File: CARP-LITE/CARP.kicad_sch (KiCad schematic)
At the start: 103 parts, among them J1 USB-C, J10 PYRO_2, J3 I2C1+3V3, J4 2S XT30, J5 UART+5V+I2C1, J6 PYRO_1, J8 PWM1+6V, J9 PWM2+6V, Q5 SQ2318CES, Q6 SQ2318CES, Q7 SQ2318CES, SW1 SW_Push, SW2 SW_Push, U1 W25Q128JVSIMTR (16MB), U2 W25Q32RVXHJQ (2MB), U3 3V3 LDO, U4 RP2350_60QFN, U5 LSM6DSO, U6 BMP390, U7 5V LDO, U8 6V LDO, Y1 ABM8-272-T3

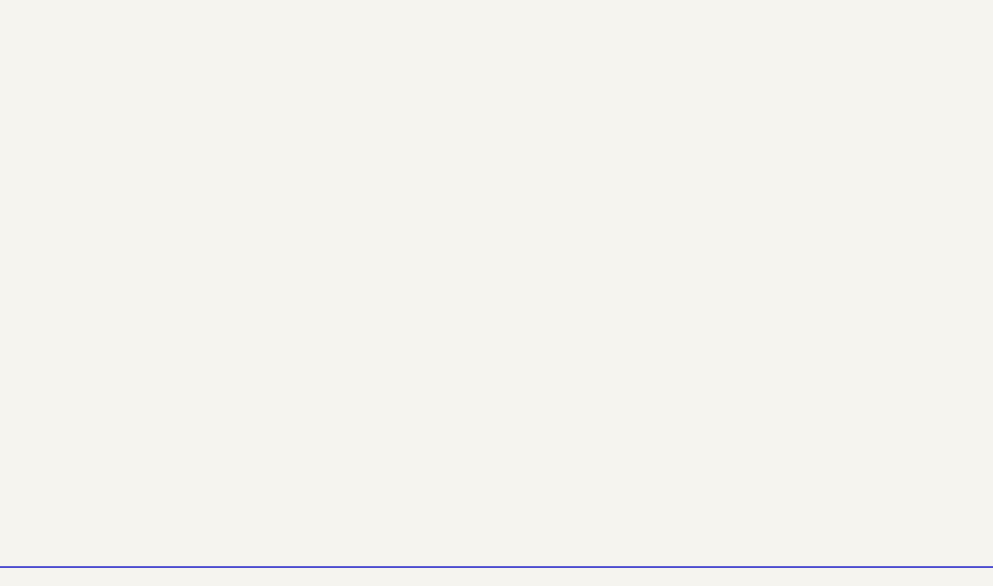
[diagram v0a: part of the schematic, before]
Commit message: Add preliminary buck design
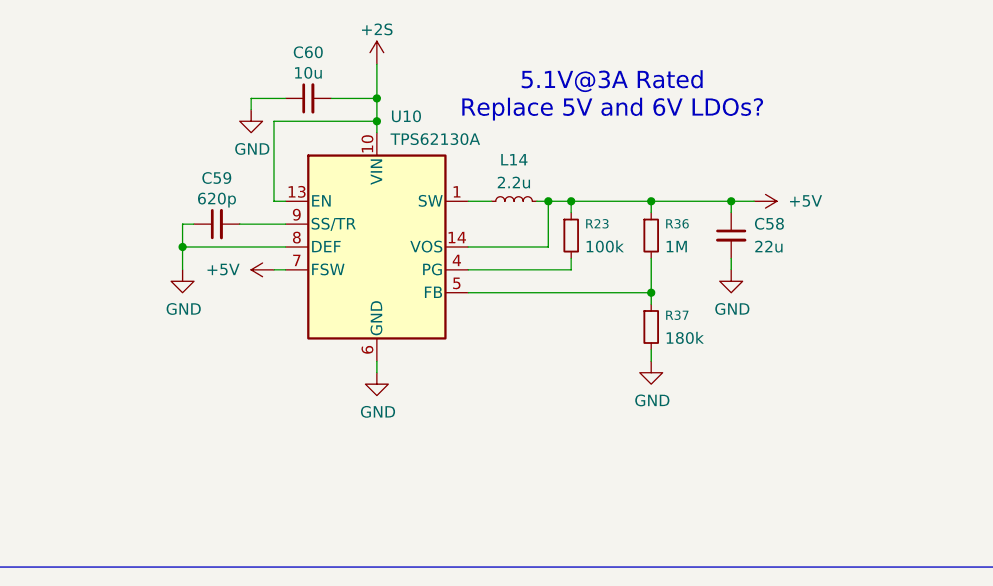
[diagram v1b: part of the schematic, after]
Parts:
- added C58: 22u, Capacitor_SMD:C_0805_2012Metric, symbol Device:C_Small
- added C59: 620p, Capacitor_SMD:C_0402_1005Metric, symbol Device:C_Small
- added C60: 10u, Capacitor_SMD:C_0805_2012Metric, symbol Device:C_Small
- added L14: 2.2u, Inductor_SMD:L_Coilcraft_XxL4020, symbol Device:L_Small
- added R23: 100k, symbol Device:R_Small
- added R36: 1M, symbol Device:R_Small
- added R37: 180k, symbol Device:R_Small
- added U10: TPS62130A, Package_DFN_QFN:VQFN-16-1EP_3x3mm_P0.5mm_EP1.68x1.68mm_ThermalVias, symbol Regulator_Switching:TPS62130A
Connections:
- net +2S: now also C60.2, U10.10 (VIN), U10.11 (VIN), U10.12 (VIN), U10.13 (EN)
- net +5V: now also C58.1, L14.2, R23.1, R36.1, U10.14 (VOS), U10.7 (FSW)
- net GND: now also C58.2, C59.1, C60.1, R37.2, U10.15 (GND), U10.16 (GND), U10.17 (GND), U10.6 (GND), U10.8 (DEF)
- new net: R36.2, R37.1, U10.5 (FB)
- new net: R23.2, U10.4 (PG)
- new net: C59.2, U10.9 (SS/TR)
- new net: L14.1, U10.1 (SW), U10.2 (SW), U10.3 (SW)
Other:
- note added: "5.1V@3A Rated Replace 5V and 6V LDOs?"

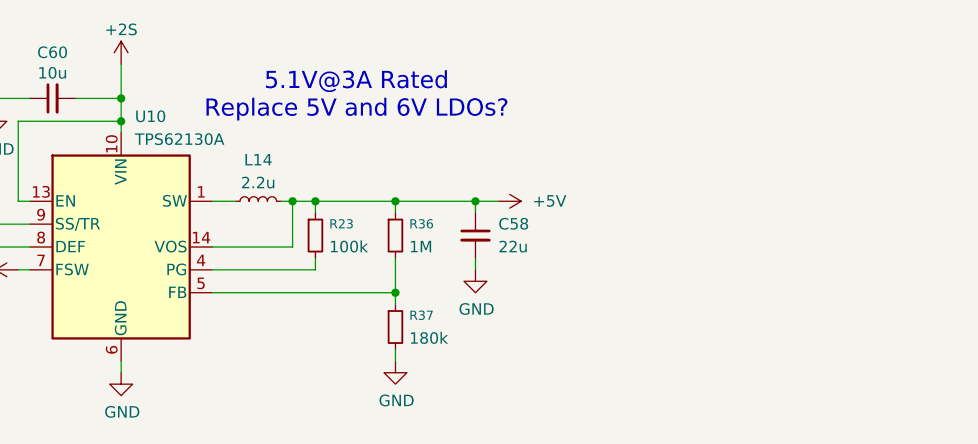
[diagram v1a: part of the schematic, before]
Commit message: add link to sim
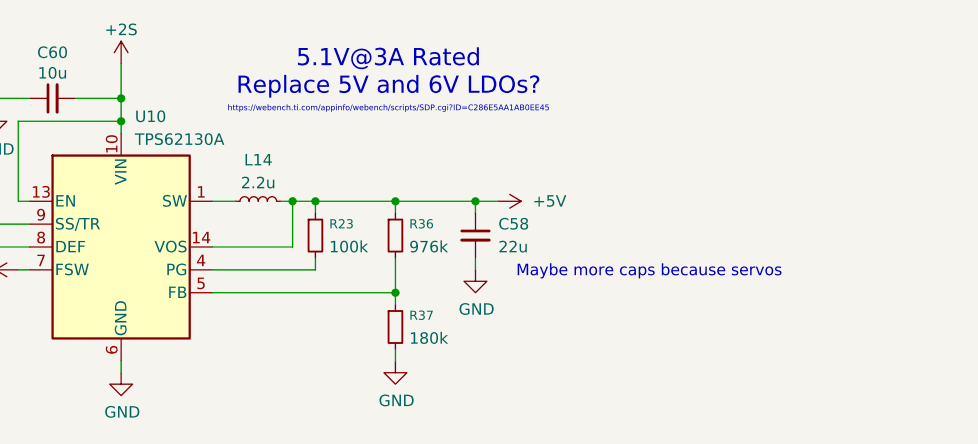
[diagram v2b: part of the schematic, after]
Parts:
- L14: MFR XEL4020-222MEB -> XGL4020-222MEC
- R36: value 1M -> 976k
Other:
- note added: "Maybe more caps because servos"
- note added: "https://webench.ti.com/appinfo/webench/scripts/SDP.cgi?ID=C286E5AA1AB0EE45"
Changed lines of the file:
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@@
 	(text "5.1V@3A Rated\nReplace 5V and 6V LDOs?"
 		(exclude_from_sim no)
-		(at 96.012 -38.354 0)
+		(at 99.568 -40.894 0)
 		(effects
 			(font
@@
 		)
 	)
+	(text "https://webench.ti.com/appinfo/webench/scripts/SDP.cgi?ID=C286E5AA1AB0EE45"
+		(exclude_from_sim no)
+		(at 99.568 -36.83 0)
+		(effects
+			(font
+				(size 0.635 0.635)
+			)
+		)
+	)
 	(text "info for choosing an NMOS:\n1.5v max gate threshold voltage\non-resistance: V_gs 2.5V or 1.8V (NO FET)\nV_ds 20V minimum"
 		(exclude_from_sim no)
@@
 		)
 	)
+	(text "Maybe more caps because servos\n"
+		(exclude_from_sim no)
+		(at 128.524 -18.796 0)
+		(effects
+			(font
+				(size 1.27 1.27)
+			)
+		)
+	)
 	(text "Power Delivery"
 		(exclude_from_sim no)
@@
 	)
 	(junction
-		(at 88.9 -26.67)
-		(diameter 0)
-		(color 0 0 0 0)
-	)
-	(junction
 		(at 303.53 26.67)
 		(diameter 0)
@@
 	)
 	(junction
+		(at 88.9 -26.67)
+		(diameter 0)
+		(color 0 0 0 0)
+	)
+	(junction
 		(at 334.01 237.49)
 		(diameter 0)
@@
 			)
 		)
-		(property "Value" "1M"
+		(property "Value" "976k"
 			(at 101.854 -21.59 0)
 			(show_name no)
@@
 			)
 		)
-		(property "MFR" "XEL4020-222MEB"
+		(property "MFR" "XGL4020-222MEC"
 			(at 85.09 -26.67 90)
 			(hide yes)

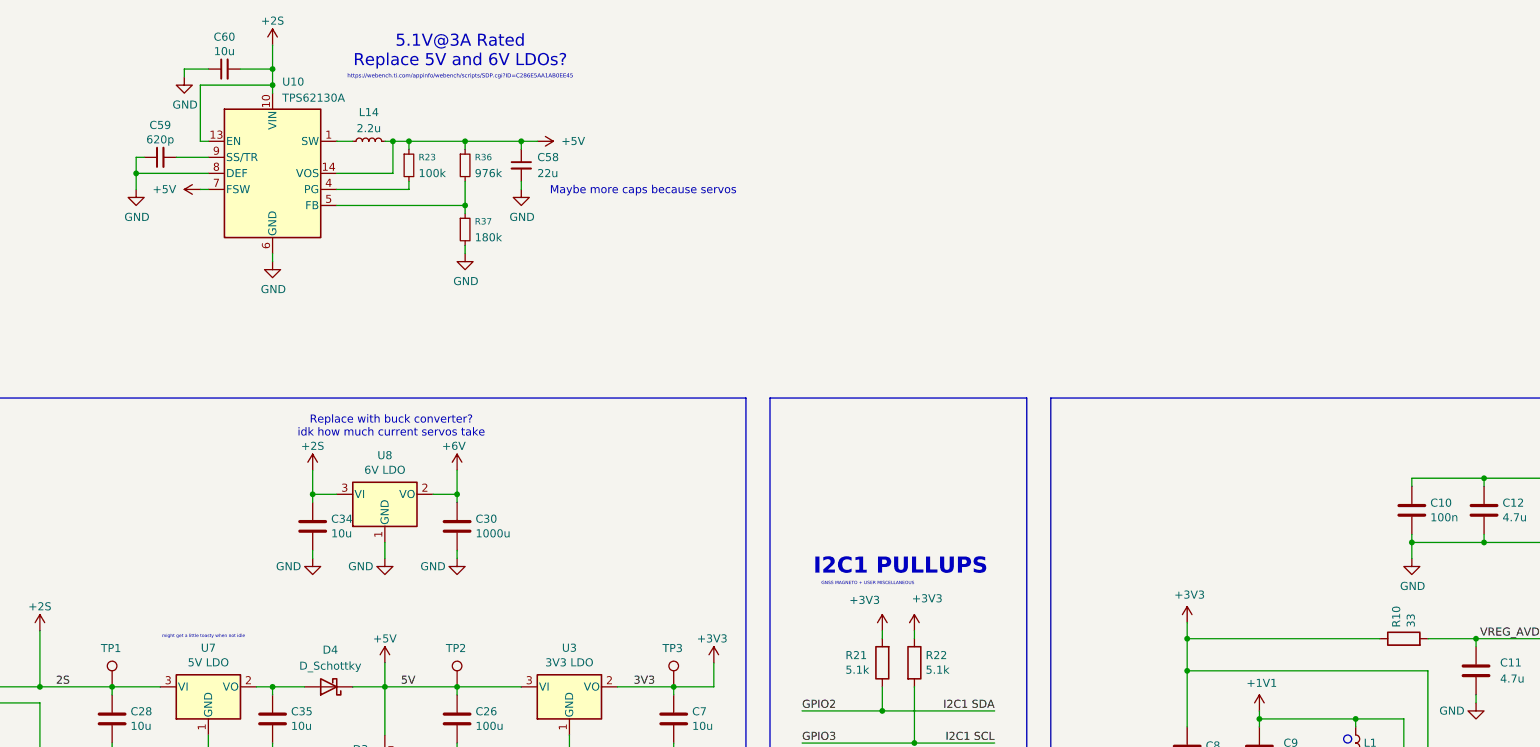
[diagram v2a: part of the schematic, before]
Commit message: move stuff around
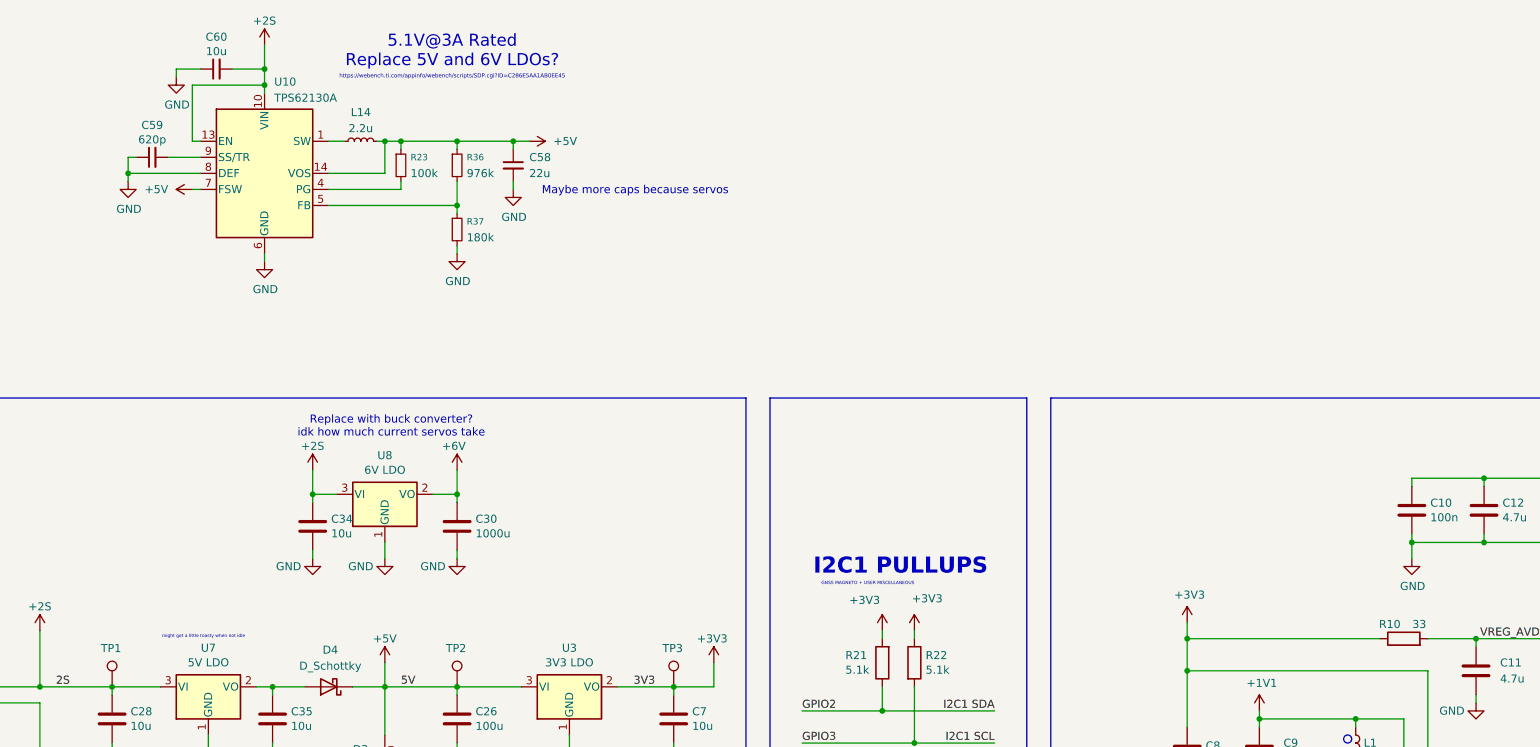
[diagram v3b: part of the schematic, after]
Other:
- moved on the sheet: C58, C59, C60, L14, R23, R36, R37, U10

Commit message: power delivery revamp
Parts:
- removed C28, C35: 10u, Capacitor_SMD:C_0603_1608Metric, symbol Device:C
- removed U7: 5V LDO, Package_TO_SOT_SMD:SOT-223-3_TabPin2, symbol Regulator_Linear:NCP1117-3.3_SOT223
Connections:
- net +2S: no longer TP1.1
- net +5V: now also R16.1; no longer C58.1, L14.2, R23.1, R36.1, U10.14 (VOS), U10.7 (FSW)
- net VBUS: no longer R16.1
- net +5V1: now reaches D4.2 (A)
- net +5V1: now also C58.1, L14.2, R23.1, R36.1, TP1.1, U10.14 (VOS), U10.7 (FSW)
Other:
- note added: "5.1V@3A Rated"
- note added: "more caps"
- note removed: "5.1V@3A Rated Replace 5V and 6V LDOs?"
- note removed: "Maybe more caps because servos"
- note removed: "might get a little toasty when not idle"
- moved on the sheet: C26, C29, C30, C34, C58, C59, C60, C7, J4, L14, R17, R18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

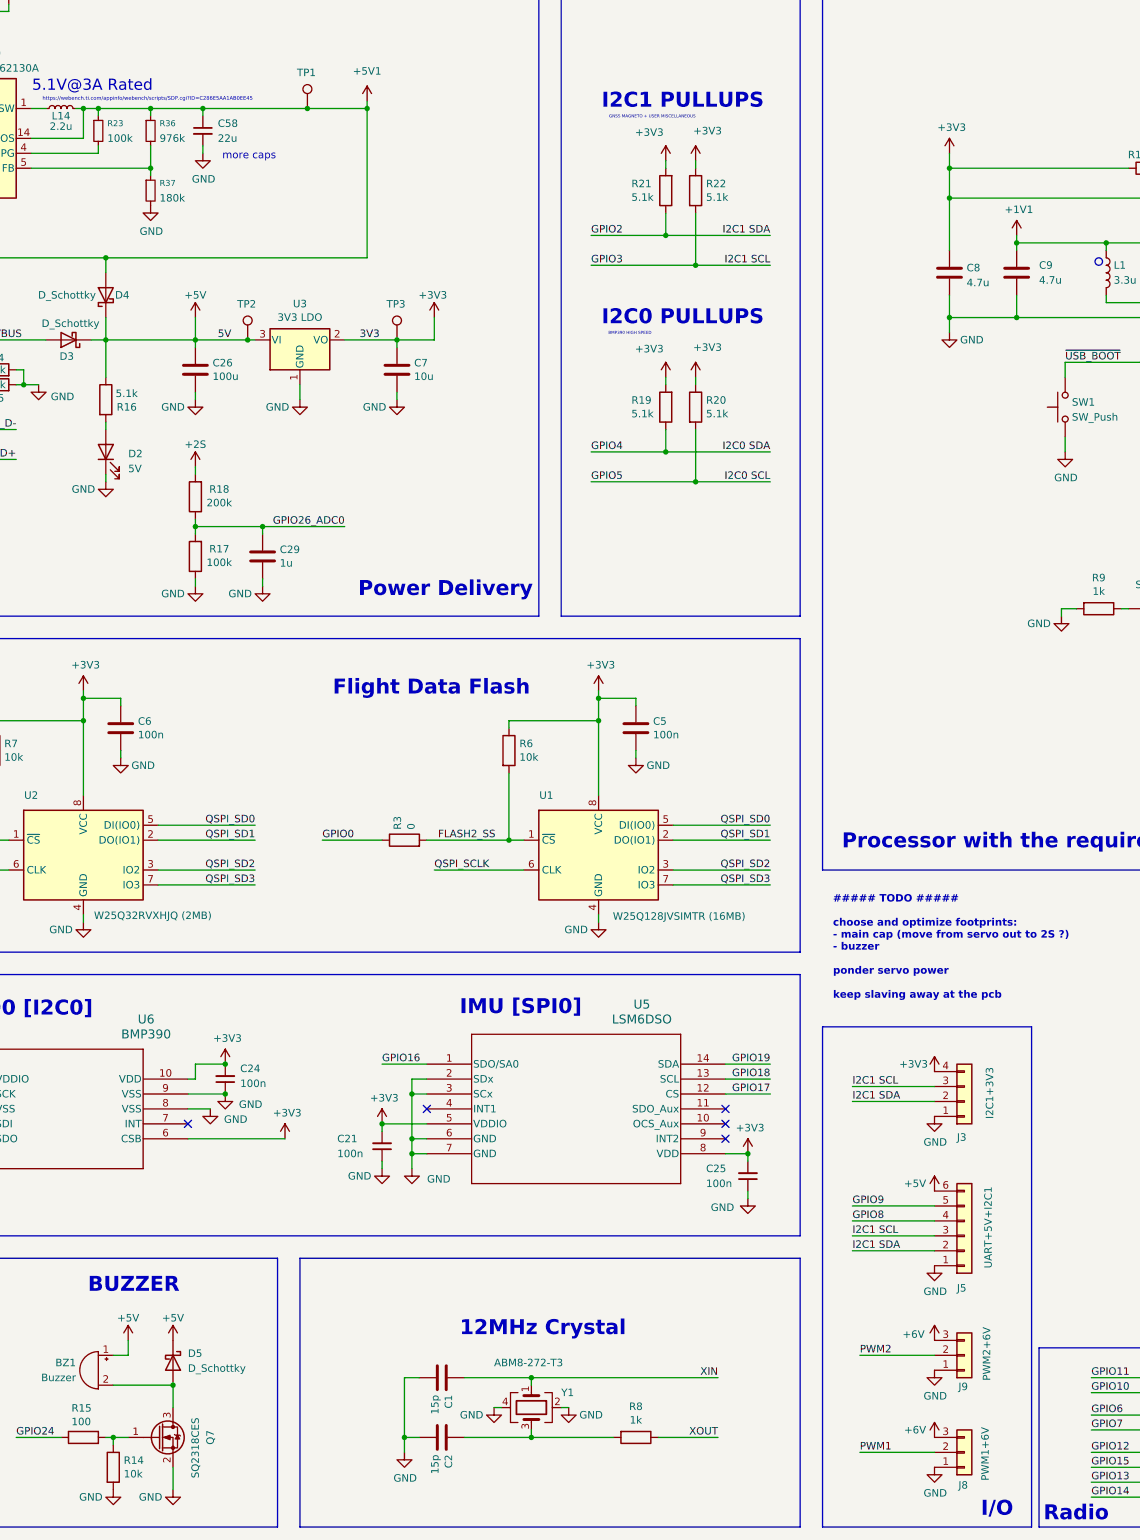
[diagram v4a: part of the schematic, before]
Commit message: add tantals
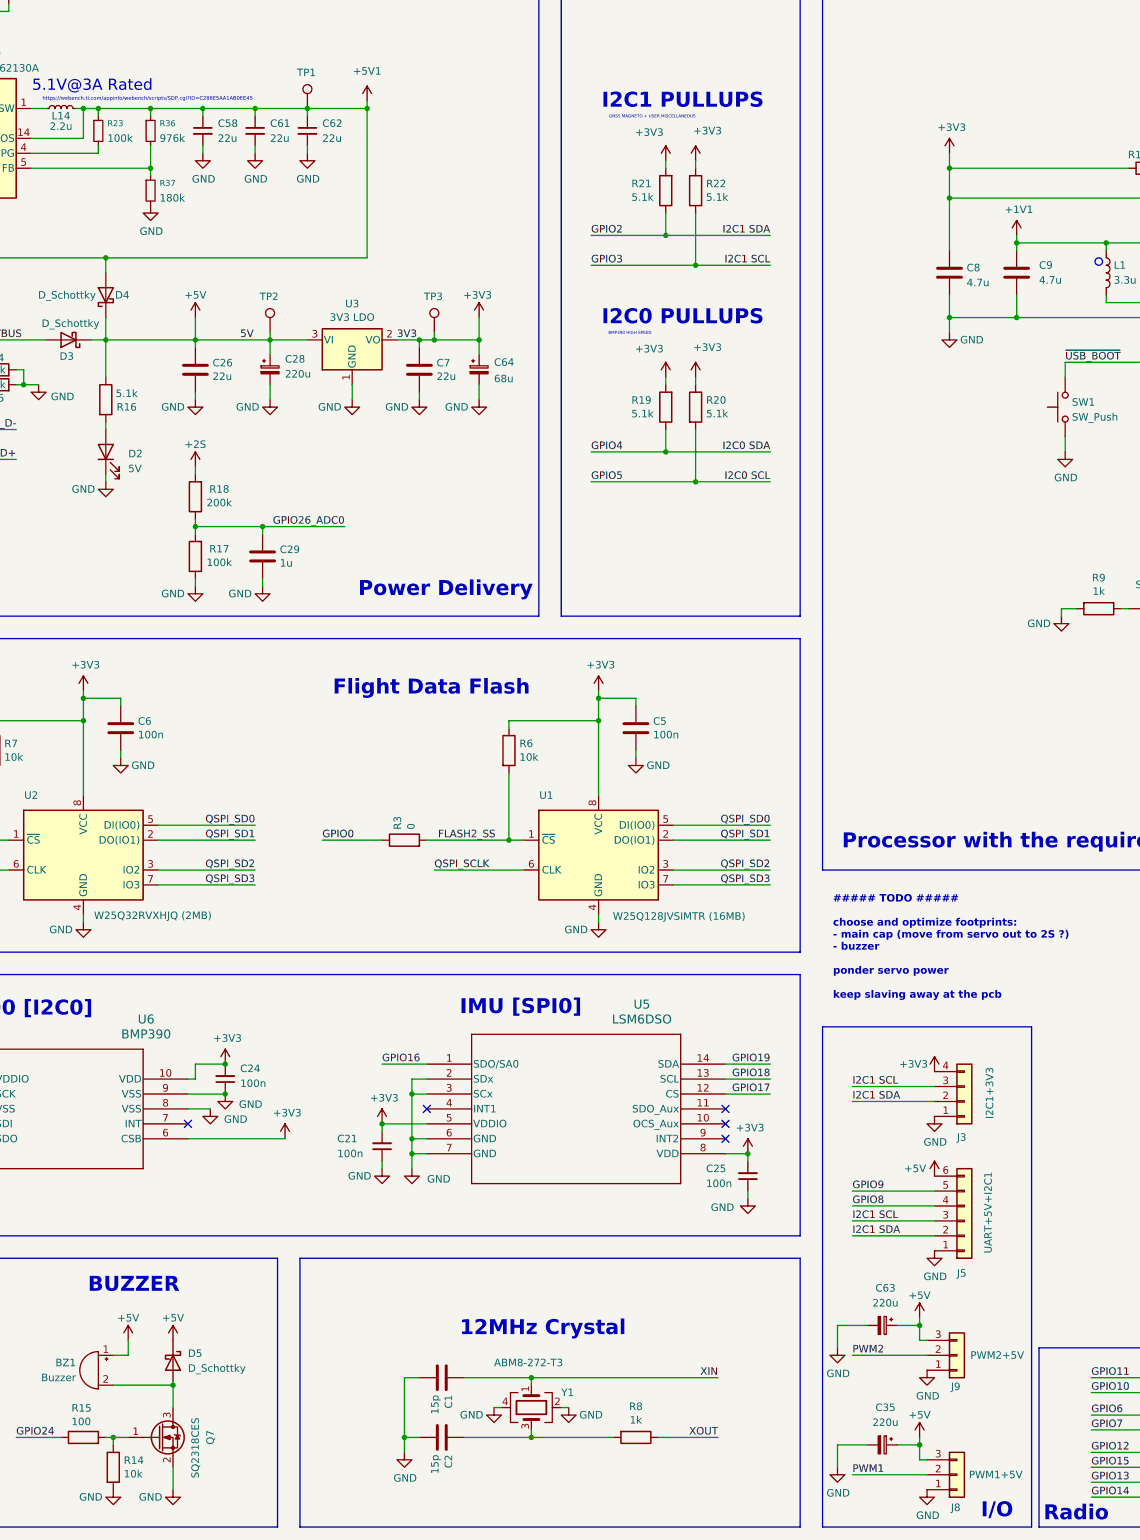
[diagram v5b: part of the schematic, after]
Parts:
- added C28, C35, C63: 220u, Capacitor_Tantalum_SMD:CP_EIA-7343-31_Kemet-D, symbol Device:C_Polarized_Small
- added C61, C62: 22u, Capacitor_SMD:C_0805_2012Metric, symbol Device:C_Small
- added C64: 68u, Capacitor_Tantalum_SMD:CP_EIA-3528-21_Kemet-B, symbol Device:C_Polarized_Small
- C26: value 100u -> 22u; footprint Capacitor_SMD:C_0603_1608Metric -> Capacitor_SMD:C_0805_2012Metric
- C7: value 10u -> 22u; footprint Capacitor_SMD:C_0603_1608Metric -> Capacitor_SMD:C_0805_2012Metric
- J8: value PWM1+6V -> PWM1+5V
- J9: value PWM2+6V -> PWM2+5V
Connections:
- net +3V3: now also C64.1
- net +5V: now also J8.3 (Pin_3), J9.3 (Pin_3), C28.1, C35.1, C63.1
- net +5V1: now also C61.1, C62.1
- net +6V: no longer J8.3 (Pin_3), J9.3 (Pin_3)
- net GND: now also C28.2, C35.2, C61.2, C62.2, C63.2, C64.2
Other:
- note removed: "more caps"
- moved on the sheet: C7, J5, J8, J9, TP2, TP3, U3

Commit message: rem ldo
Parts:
- removed C30: 1000u, Capacitor_SMD:CP_Elec_10x10, symbol Device:C
- removed C34: 10u, Capacitor_SMD:C_0603_1608Metric, symbol Device:C
- removed U8: 6V LDO, Package_TO_SOT_SMD:SOT-223-3_TabPin2, symbol Regulator_Linear:NCP1117-3.3_SOT223
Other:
- note removed: "Replace with buck converter? idk how much current servos take"
